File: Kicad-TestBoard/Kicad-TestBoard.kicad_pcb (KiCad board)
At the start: 2 copper layers, 50 x 100 mm, 38 parts, among them CON1 Power 6V-12V, J1 DB9 RS-232 Female, P1 Power 6V-12V, P2 Debug, P4 Arduino, P5 AVR Programmer, P6 RS-232, Q1 Association, Q2 On_Sleep, Q3 Commissioning, SW1 Reset, SW2 Commissioning, U1 78L05, U2 MAX232

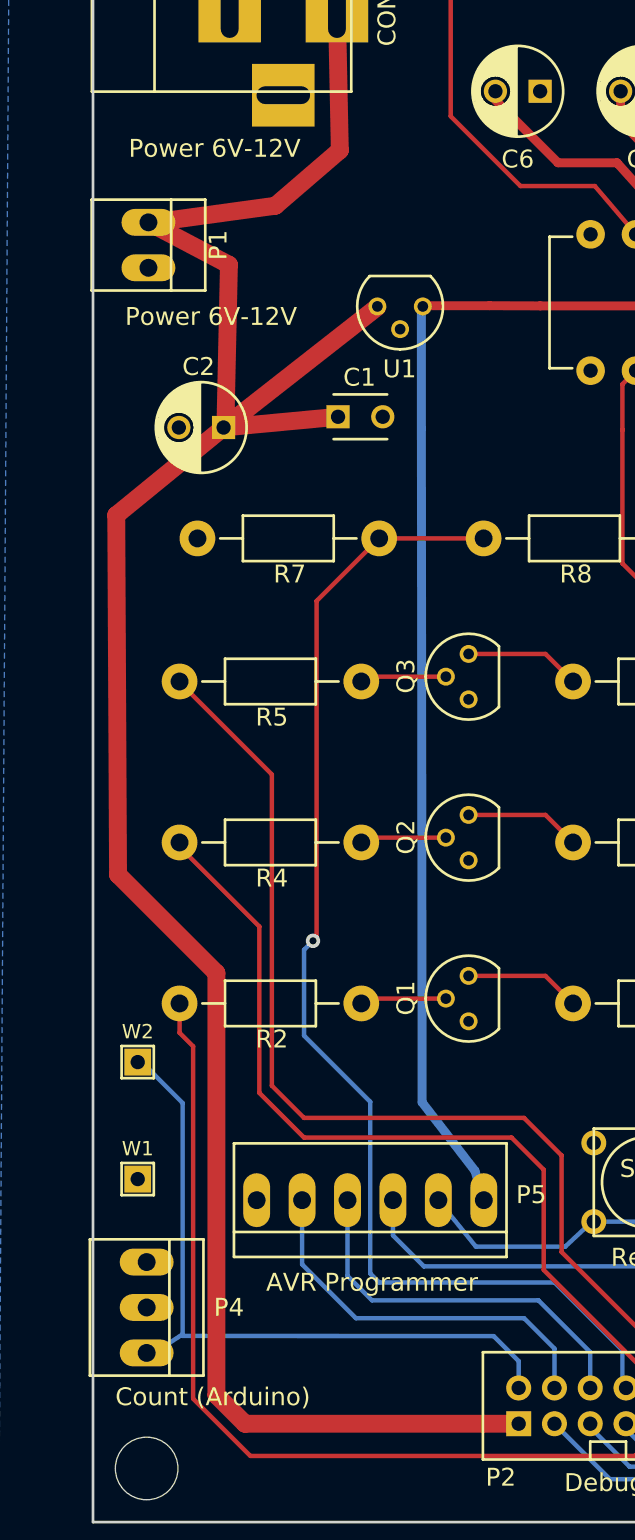
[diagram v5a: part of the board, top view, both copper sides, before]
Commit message: Add power jumper to disconnect testboard power from meter when battery is present in the latter.
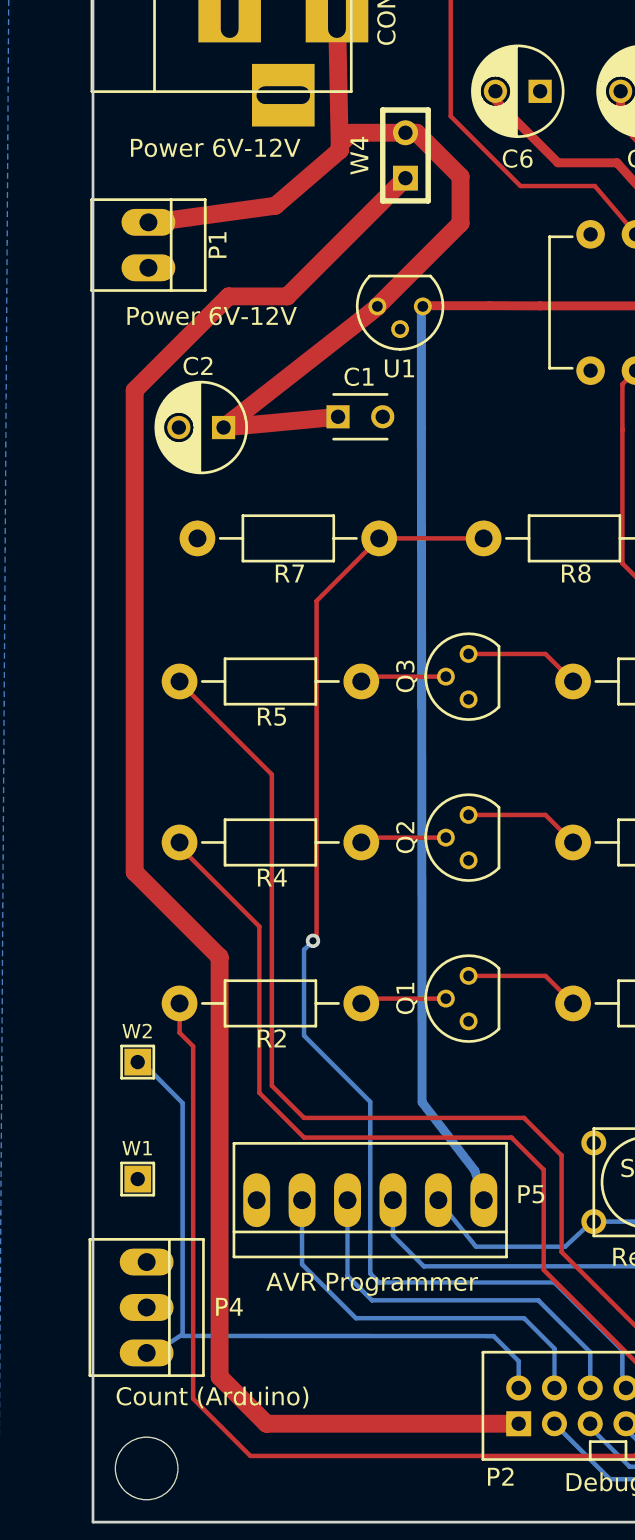
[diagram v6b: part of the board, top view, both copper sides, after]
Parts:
- added W4: Jumper, Testboard:SIL-2, F.Cu at (167.5, 73.6)
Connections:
- C1 pad 1: /Battery -> Net-(C1-Pad1)
- C2 pad 1: /Battery -> Net-(C1-Pad1)
- CON1 pad 1: /Battery -> Net-(C1-Pad1)
- P1 pad 1: /Battery -> Net-(C1-Pad1)
- U1 pad VI: /Battery -> Net-(C1-Pad1)
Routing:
- net Net-(C1-Pad1): track 0.00 -> 54.9 mm
- net /Battery: track 128.5 -> 95.0 mm
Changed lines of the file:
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@@
-(kicad_pcb (version 4) (host pcbnew 4.0.4+e1-6308~48~ubuntu14.04.1-stable)
+(kicad_pcb (version 4) (host pcbnew 4.0.5-e0-6337~49~ubuntu14.04.1)
   (general
-    (links 72)
+    (links 73)
     (no_connects 0)
-    (area 143.5 46.5 207.200001 156.000001)
+    (area 149.924999 49.924999 200.075001 150.075001)
     (thickness 1.6)
     (drawings 17)
-    (tracks 183)
+    (tracks 190)
     (zones 0)
-    (modules 38)
-    (nets 42)
+    (modules 39)
+    (nets 43)
   )
   (page A4)
@@
   )
   (setup
-    (last_trace_width 0.25)
+    (last_trace_width 1)
     (user_trace_width 0.5)
     (user_trace_width 1)
@@
   (net 40 "Net-(P4-Pad2)")
   (net 41 "Net-(U2-Pad11)")
+  (net 42 "Net-(C1-Pad1)")
   (net_class Default "This is the default net class."
     (clearance 0.2)
@@
     (add_net /Tx)
     (add_net Earth)
+    (add_net "Net-(C1-Pad1)")
     (add_net "Net-(C3-Pad1)")
     (add_net "Net-(C3-Pad2)")
@@
     (fp_line (start 2.75 1.25) (end -0.25 1.25) (layer F.SilkS) (width 0.15))
     (pad 1 thru_hole rect (at 0 0) (size 1.3 1.3) (drill 0.8) (layers *.Cu *.Mask F.SilkS)
-      (net 1 /Battery))
+      (net 42 "Net-(C1-Pad1)"))
     (pad 2 thru_hole circle (at 2.5 0) (size 1.3 1.3) (drill 0.8) (layers *.Cu *.Mask F.SilkS)
       (net 2 Earth))
@@
     (fp_circle (center 1.25 0) (end 1.25 -2.8) (layer F.CrtYd) (width 0.05))
     (pad 1 thru_hole rect (at 0 0 180) (size 1.3 1.3) (drill 0.8) (layers *.Cu *.Mask F.SilkS)
-      (net 1 /Battery))
+      (net 42 "Net-(C1-Pad1)"))
     (pad 2 thru_hole circle (at 2.5 0 180) (size 1.3 1.3) (drill 0.8) (layers *.Cu *.Mask F.SilkS)
       (net 2 Earth))
@@
     (fp_line (start 7.00024 -4.50088) (end -7.50062 -4.50088) (layer F.SilkS) (width 0.15))
     (pad 1 thru_hole rect (at 6.20014 0) (size 3.50012 3.50012) (drill oval 1 3) (layers *.Cu *.Mask F.SilkS)
-      (net 1 /Battery))
+      (net 42 "Net-(C1-Pad1)"))
     (pad 2 thru_hole rect (at 0.20066 0) (size 3.50012 3.50012) (drill oval 1 3) (layers *.Cu *.Mask F.SilkS)
       (net 2 Earth))
@@
     (fp_line (start 2.54 -3.175) (end 2.54 3.175) (layer F.SilkS) (width 0.15))
     (pad 1 thru_hole oval (at -1.27 0 270) (size 1.50622 3.01498) (drill 1) (layers *.Cu *.Mask)
-      (net 1 /Battery))
+      (net 42 "Net-(C1-Pad1)"))
     (pad 2 thru_hole oval (at 1.27 0 270) (size 1.50622 3.01498) (drill 1) (layers *.Cu *.Mask)
       (net 2 Earth))
@@
       (net 2 Earth))
     (pad VI thru_hole circle (at 2.54 0 270) (size 1.00076 1.00076) (drill 0.6) (layers *.Cu *.Mask F.SilkS)
-      (net 1 /Battery))
+      (net 42 "Net-(C1-Pad1)"))
     (pad VO thru_hole circle (at 0 0 270) (size 1.00076 1.00076) (drill 0.6) (layers *.Cu *.Mask F.SilkS)
       (net 3 VCC))
@@
     )
   )
+  (module Testboard:SIL-2 (layer F.Cu)
+    (at 167.47 73.59 90)
+    (descr "Connecteurs 2 pins")
+    (tags "CONN DEV")
+    (fp_text reference W4 (at 0 -2.54 90) (layer F.SilkS)
+      (effects (font (size 1 1) (thickness 0.15)))
+    )
+    (fp_text value Jumper (at 0 -2.54 90) (layer F.SilkS) hide
+      (effects (font (size 1.524 1.016) (thickness 0.3048)))
+    )
+    (fp_line (start -2.54 1.27) (end -2.54 -1.27) (layer F.SilkS) (width 0.3048))
+    (fp_line (start -2.54 -1.27) (end 2.54 -1.27) (layer F.SilkS) (width 0.3048))
+    (fp_line (start 2.54 -1.27) (end 2.54 1.27) (layer F.SilkS) (width 0.3048))
+    (fp_line (start 2.54 1.27) (end -2.54 1.27) (layer F.SilkS) (width 0.3048))
+    (pad 1 thru_hole rect (at -1.27 0 90) (size 1.397 1.397) (drill 0.8) (layers *.Cu *.Mask F.SilkS)
+      (net 1 /Battery))
+    (pad 2 thru_hole circle (at 1.27 0 90) (size 1.397 1.397) (drill 0.8) (layers *.Cu *.Mask F.SilkS)
+      (net 42 "Net-(C1-Pad1)"))
+  )
   (gr_text "Do NOT link if\nXBee present" (at 189.8 91.3) (layer F.SilkS)
     (effects (font (size 1 1) (thickness 0.25)))
@@
   (gr_line (start 200 50) (end 200 150) (angle 90) (layer Edge.Cuts) (width 0.15))
   (gr_line (start 150 50) (end 200 50) (angle 90) (layer Edge.Cuts) (width 0.15))
-  (segment (start 163.7 88.2) (end 157.3 88.8) (width 1) (layer F.Cu) (net 1))
-  (segment (start 157.3 88.8) (end 157.4 88.9) (width 1) (layer F.Cu) (net 1) (status 10))
-  (segment (start 157.6 79.7) (end 153.1 77.33) (width 1) (layer F.Cu) (net 1) (status 20))
-  (segment (start 157.4 88.9) (end 157.6 79.7) (width 1) (layer F.Cu) (net 1))
-  (segment (start 163.64014 65.52) (end 163.8 73.3) (width 1) (layer F.Cu) (net 1))
-  (segment (start 163.8 73.3) (end 160.2 76.4) (width 1) (layer F.Cu) (net 1))
-  (segment (start 160.2 76.4) (end 152.9 77.4) (width 1) (layer F.Cu) (net 1))
-  (segment (start 165.89 82.07) (end 157.3 88.8) (width 1) (layer F.Cu) (net 1) (status 10))
-  (segment (start 173.8 144.5) (end 158.5 144.5) (width 1) (layer F.Cu) (net 1) (status 10))
-  (segment (start 151.3 93.7) (end 157.3 88.8) (width 1) (layer F.Cu) (net 1) (status 20))
-  (segment (start 151.4 113.8) (end 151.3 93.7) (width 1) (layer F.Cu) (net 1))
-  (segment (start 156.9 119.3) (end 151.4 113.8) (width 1) (layer F.Cu) (net 1))
-  (segment (start 156.9 142.9) (end 156.9 119.3) (width 1) (layer F.Cu) (net 1))
-  (segment (start 158.5 144.5) (end 156.9 142.9) (width 1) (layer F.Cu) (net 1))
-  (segment (start 157.3 88.8) (end 157.3 88.8) (width 1) (layer F.Cu) (net 1) (status 20))
+  (segment (start 173.8 144.5) (end 159.7 144.5) (width 1) (layer F.Cu) (net 1))
+  (segment (start 160.86 81.47) (end 167.47 74.86) (width 1) (layer F.Cu) (net 1))
+  (segment (start 157.58 81.47) (end 160.86 81.47) (width 1) (layer F.Cu) (net 1))
+  (segment (start 152.33 86.72) (end 157.58 81.47) (width 1) (layer F.Cu) (net 1))
+  (segment (start 152.33 113.66) (end 152.33 86.72) (width 1) (layer F.Cu) (net 1))
+  (segment (start 157.08 118.41) (end 152.33 113.66) (width 1) (layer F.Cu) (net 1))
+  (segment (start 157.08 141.88) (end 157.08 118.41) (width 1) (layer F.Cu) (net 1))
+  (segment (start 159.7 144.5) (end 157.08 141.88) (width 1) (layer F.Cu) (net 1))
   (segment (start 168.36 88.85) (end 168.36 81.83) (width 0.5) (layer B.Cu) (net 3) (status 20))
   (segment (start 168.43 81.99) (end 172.18 81.99) (width 0.5) (layer F.Cu) (net 3) (status 10))
@@
   (segment (start 158.8 146.3) (end 180.3 146.3) (width 0.25) (layer F.Cu) (net 39))
   (segment (start 154.84 122.64) (end 155.6 123.4) (width 0.25) (layer F.Cu) (net 39))
+  (segment (start 167.47 72.32) (end 168.1 72.32) (width 1) (layer F.Cu) (net 42))
+  (segment (start 168.1 72.32) (end 170.55 74.77) (width 1) (layer F.Cu) (net 42))
+  (segment (start 170.55 77.38) (end 165.9 82.03) (width 1) (layer F.Cu) (net 42))
+  (segment (start 170.55 74.77) (end 170.55 77.38) (width 1) (layer F.Cu) (net 42))
+  (segment (start 163.8 72.97) (end 163.8 73.3) (width 1) (layer F.Cu) (net 42))
+  (segment (start 164.45 72.32) (end 163.8 72.97) (width 1) (layer F.Cu) (net 42))
+  (segment (start 167.47 72.32) (end 164.45 72.32) (width 1) (layer F.Cu) (net 42))
+  (segment (start 163.8 73.3) (end 160.2 76.4) (width 1) (layer F.Cu) (net 42))
+  (segment (start 163.7 88.2) (end 157.3 88.8) (width 1) (layer F.Cu) (net 42))
+  (segment (start 157.3 88.8) (end 157.4 88.9) (width 1) (layer F.Cu) (net 42) (status 10))
+  (segment (start 163.64014 65.52) (end 163.8 73.3) (width 1) (layer F.Cu) (net 42))
+  (segment (start 160.2 76.4) (end 152.9 77.4) (width 1) (layer F.Cu) (net 42))
+  (segment (start 165.89 82.07) (end 157.3 88.8) (width 1) (layer F.Cu) (net 42) (status 10))
+  (segment (start 157.3 88.8) (end 157.3 88.8) (width 1) (layer F.Cu) (net 42) (status 20))
   (zone (net 2) (net_name Earth) (layer B.Cu) (hatch edge 0.508)
     (connect_pads (clearance 0.508))

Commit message: Minor mods to PCB for kicad Testboard
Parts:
- moved W4 70.9 mm to (164.6, 144.5), turned to 180 degrees
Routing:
- net /Battery: track 95.0 -> 7.91 mm
- net Net-(C1-Pad1): track 54.9 -> 131.5 mm
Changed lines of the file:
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@@
   (general
     (links 73)
-    (no_connects 0)
-    (area 149.924999 49.924999 200.075001 150.075001)
+    (no_connects 1)
+    (area 143.5 46.5 207.200001 156.000001)
     (thickness 1.6)
     (drawings 17)
-    (tracks 190)
+    (tracks 192)
     (zones 0)
     (modules 39)
@@
   )
   (setup
-    (last_trace_width 1)
+    (last_trace_width 0.25)
     (user_trace_width 0.5)
     (user_trace_width 1)
@@
   )
   (module Testboard:SIL-2 (layer F.Cu)
-    (at 167.47 73.59 90)
+    (at 164.64 144.46 180)
     (descr "Connecteurs 2 pins")
     (tags "CONN DEV")
-    (fp_text reference W4 (at 0 -2.54 90) (layer F.SilkS)
-      (effects (font (size 1 1) (thickness 0.15)))
-    )
-    (fp_text value Jumper (at 0 -2.54 90) (layer F.SilkS) hide
+    (fp_text reference W4 (at 0 -2.54 180) (layer F.SilkS)
+      (effects (font (size 1 1) (thickness 0.15)))
+    )
+    (fp_text value Jumper (at 0 -2.54 180) (layer F.SilkS) hide
       (effects (font (size 1.524 1.016) (thickness 0.3048)))
     )
@@
     (fp_line (start 2.54 -1.27) (end 2.54 1.27) (layer F.SilkS) (width 0.3048))
     (fp_line (start 2.54 1.27) (end -2.54 1.27) (layer F.SilkS) (width 0.3048))
-    (pad 1 thru_hole rect (at -1.27 0 90) (size 1.397 1.397) (drill 0.8) (layers *.Cu *.Mask F.SilkS)
+    (pad 1 thru_hole rect (at -1.27 0 180) (size 1.397 1.397) (drill 0.8) (layers *.Cu *.Mask F.SilkS)
       (net 1 /Battery))
-    (pad 2 thru_hole circle (at 1.27 0 90) (size 1.397 1.397) (drill 0.8) (layers *.Cu *.Mask F.SilkS)
+    (pad 2 thru_hole circle (at 1.27 0 180) (size 1.397 1.397) (drill 0.8) (layers *.Cu *.Mask F.SilkS)
       (net 42 "Net-(C1-Pad1)"))
   )
@@
   (gr_line (start 200 50) (end 200 150) (angle 90) (layer Edge.Cuts) (width 0.15))
   (gr_line (start 150 50) (end 200 50) (angle 90) (layer Edge.Cuts) (width 0.15))
-  (segment (start 173.8 144.5) (end 159.7 144.5) (width 1) (layer F.Cu) (net 1))
-  (segment (start 160.86 81.47) (end 167.47 74.86) (width 1) (layer F.Cu) (net 1))
-  (segment (start 157.58 81.47) (end 160.86 81.47) (width 1) (layer F.Cu) (net 1))
-  (segment (start 152.33 86.72) (end 157.58 81.47) (width 1) (layer F.Cu) (net 1))
-  (segment (start 152.33 113.66) (end 152.33 86.72) (width 1) (layer F.Cu) (net 1))
-  (segment (start 157.08 118.41) (end 152.33 113.66) (width 1) (layer F.Cu) (net 1))
-  (segment (start 157.08 141.88) (end 157.08 118.41) (width 1) (layer F.Cu) (net 1))
-  (segment (start 159.7 144.5) (end 157.08 141.88) (width 1) (layer F.Cu) (net 1))
+  (segment (start 165.91 144.46) (end 173.76 144.46) (width 1) (layer F.Cu) (net 1))
+  (segment (start 173.76 144.46) (end 173.8 144.5) (width 1) (layer F.Cu) (net 1))
   (segment (start 168.36 88.85) (end 168.36 81.83) (width 0.5) (layer B.Cu) (net 3) (status 20))
   (segment (start 168.43 81.99) (end 172.18 81.99) (width 0.5) (layer F.Cu) (net 3) (status 10))
@@
   (segment (start 179.6 96.4) (end 179.6 88.94) (width 0.25) (layer F.Cu) (net 20))
   (segment (start 179.6 88.94) (end 179.6 88.92) (width 0.25) (layer F.Cu) (net 20))
-  (segment (start 154.84 103) (end 154.84 103.04) (width 0.25) (layer F.Cu) (net 21))
-  (segment (start 154.84 103.04) (end 160 108.2) (width 0.25) (layer F.Cu) (net 21))
-  (segment (start 160 108.2) (end 160 125.6) (width 0.25) (layer F.Cu) (net 21))
+  (segment (start 154.84 109.35) (end 154.84 103) (width 0.25) (layer F.Cu) (net 21))
+  (segment (start 154.84 109.31) (end 154.84 109.35) (width 0.25) (layer F.Cu) (net 21))
+  (segment (start 154.84 109.35) (end 160 114.51) (width 0.25) (layer F.Cu) (net 21))
+  (segment (start 160 114.51) (end 160 125.6) (width 0.25) (layer F.Cu) (net 21))
   (segment (start 160 125.6) (end 161.8 127.4) (width 0.25) (layer F.Cu) (net 21))
   (segment (start 161.8 127.4) (end 174.1 127.4) (width 0.25) (layer F.Cu) (net 21))
@@
   (segment (start 158.8 146.3) (end 180.3 146.3) (width 0.25) (layer F.Cu) (net 39))
   (segment (start 154.84 122.64) (end 155.6 123.4) (width 0.25) (layer F.Cu) (net 39))
+  (segment (start 163.22 144.46) (end 159.7 144.5) (width 1) (layer F.Cu) (net 42))
+  (segment (start 157.58 81.47) (end 157.62 76.72) (width 1) (layer F.Cu) (net 42))
+  (segment (start 152.33 86.72) (end 157.58 81.47) (width 1) (layer F.Cu) (net 42))
+  (segment (start 152.33 113.66) (end 152.33 86.72) (width 1) (layer F.Cu) (net 42))
+  (segment (start 157.08 118.41) (end 152.33 113.66) (width 1) (layer F.Cu) (net 42))
+  (segment (start 157.08 141.88) (end 157.08 118.41) (width 1) (layer F.Cu) (net 42))
+  (segment (start 159.7 144.5) (end 157.08 141.88) (width 1) (layer F.Cu) (net 42))
   (segment (start 167.47 72.32) (end 168.1 72.32) (width 1) (layer F.Cu) (net 42))
   (segment (start 168.1 72.32) (end 170.55 74.77) (width 1) (layer F.Cu) (net 42))

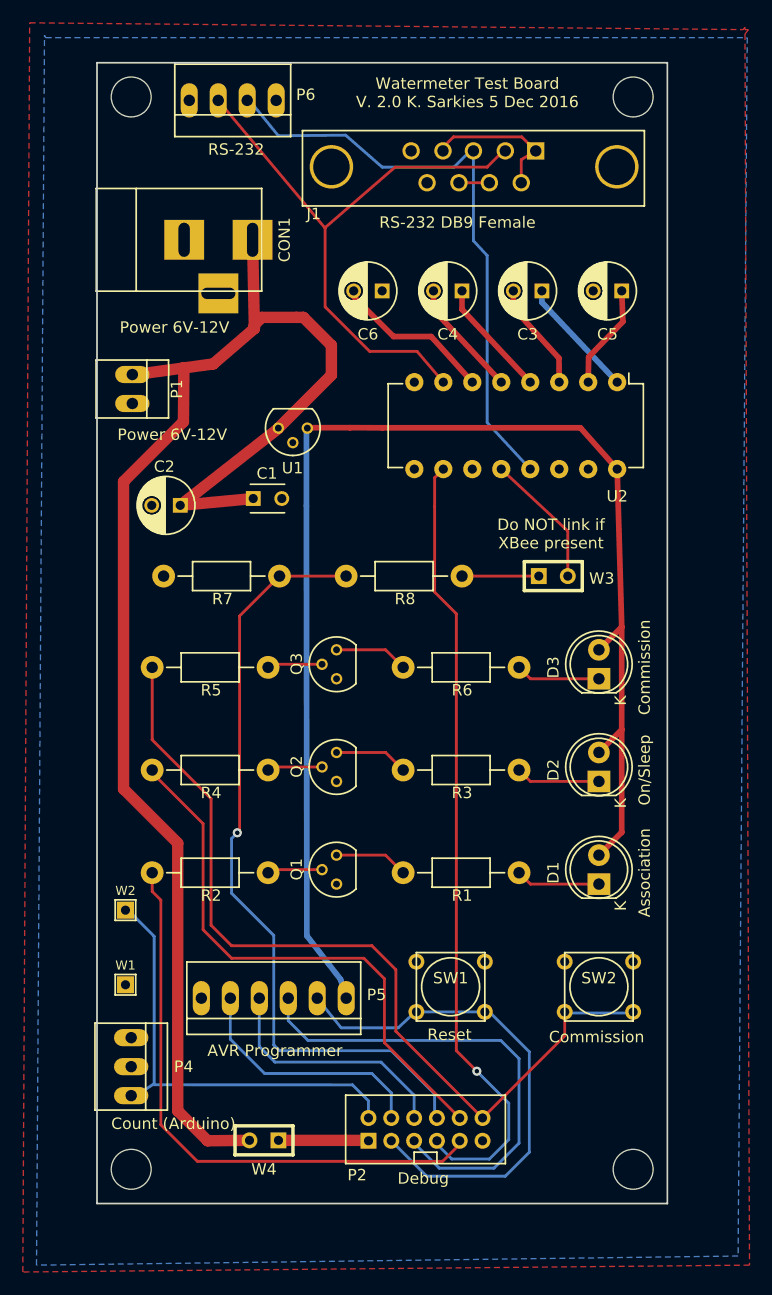
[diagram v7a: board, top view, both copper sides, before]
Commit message: Add logo to testboard. Add a README.
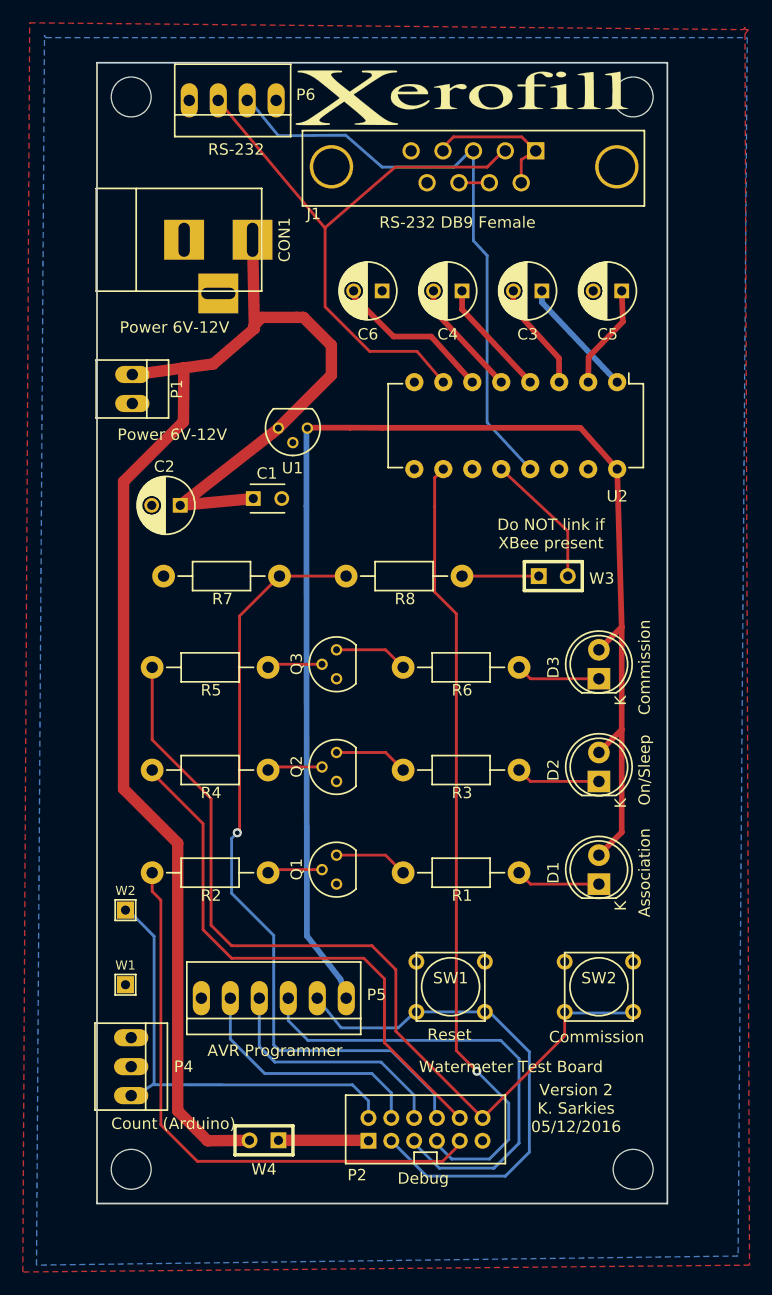
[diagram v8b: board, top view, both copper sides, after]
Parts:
- added G***: LOGO, photodiode:Xerofill-Logo-Small, F.Cu at (181.9, 53.0)
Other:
- board text added: "Version 2 K. Sarkies 05/12/2016"
- board text added: "Watermeter Test Board"
- board text removed: "Watermeter Test Board V. 2.0 K. Sarkies 5 Dec 2016"
